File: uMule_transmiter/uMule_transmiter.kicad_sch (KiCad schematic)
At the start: 46 parts, among them J1 Test_Point_Sine, J2 Test_Point_Cos, U1 LM324, U2 LM324

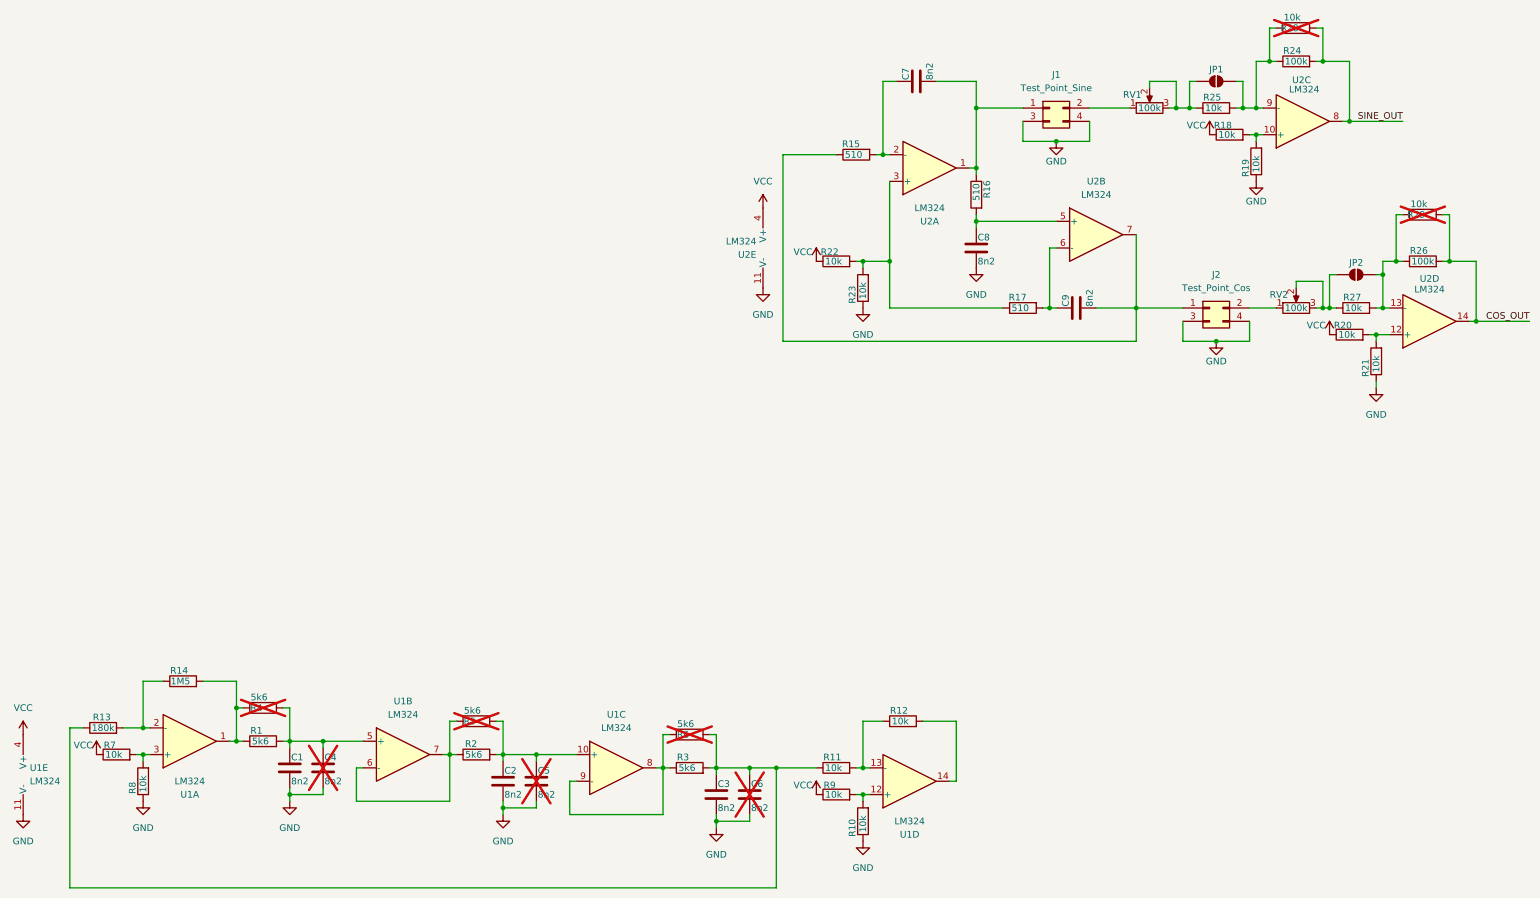
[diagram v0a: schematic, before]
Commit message: Transmiter board finnished. Ready for JLCPCB
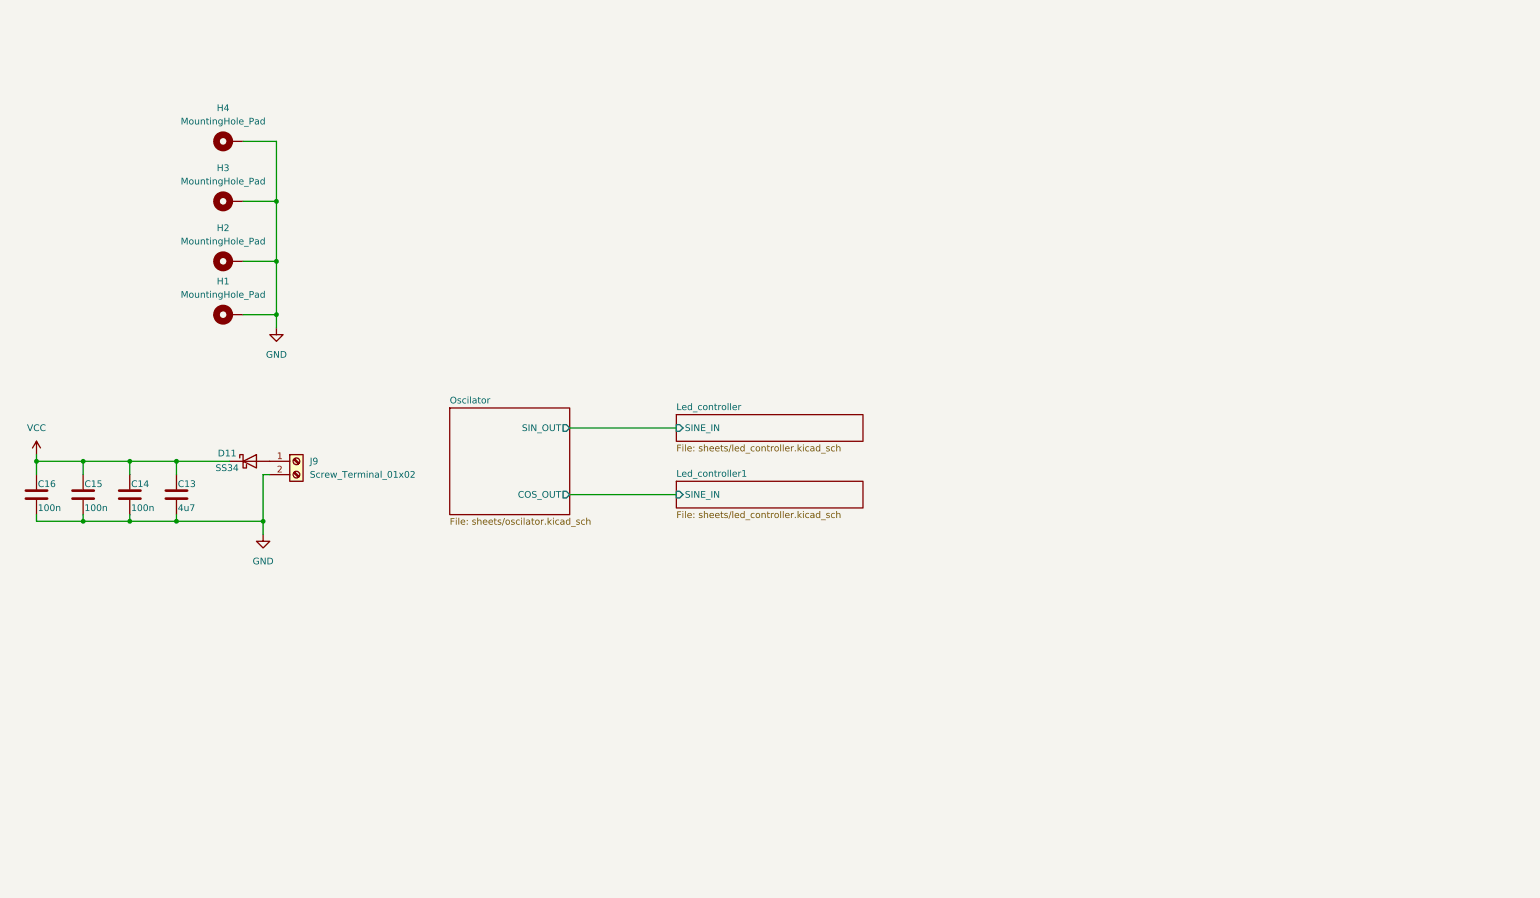
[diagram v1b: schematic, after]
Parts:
- removed C1, C2, C3, C7, C8, C9: 8n2, Capacitor_SMD:C_0603_1608Metric_Pad1.08x0.95mm_HandSolder, symbol Device:C
- removed C4, C5, C6: 8n2, Capacitor_THT:C_Axial_L5.1mm_D3.1mm_P7.50mm_Horizontal, symbol Device:C
- removed J1: Test_Point_Sine, Connector_PinHeader_2.54mm:PinHeader_2x02_P2.54mm_Vertical, symbol Connector_Generic:Conn_02x02_Odd_Even
- removed J2: Test_Point_Cos, Connector_PinHeader_2.54mm:PinHeader_2x02_P2.54mm_Vertical, symbol Connector_Generic:Conn_02x02_Odd_Even
- removed JP1, JP2: SolderJumper_2_Open, Jumper:SolderJumper-2_P1.3mm_Open_RoundedPad1.0x1.5mm, symbol Jumper:SolderJumper_2_Open
- removed R1, R2, R3: 5k6, Resistor_SMD:R_0603_1608Metric_Pad0.98x0.95mm_HandSolder, symbol Device:R
- removed R10, R11, R12, R18, R19, R20, R21, R22, R23, R25, R27, R7, R8, R9: 10k, Resistor_SMD:R_0603_1608Metric_Pad0.98x0.95mm_HandSolder, symbol Device:R
- removed R13: 180k, Resistor_THT:R_Axial_DIN0207_L6.3mm_D2.5mm_P7.62mm_Horizontal, symbol Device:R
- removed R14: 1M5, Resistor_THT:R_Axial_DIN0207_L6.3mm_D2.5mm_P7.62mm_Horizontal, symbol Device:R
- removed R15, R16, R17: 510, Resistor_SMD:R_0603_1608Metric_Pad0.98x0.95mm_HandSolder, symbol Device:R
- removed R24, R26: 100k, Resistor_SMD:R_0603_1608Metric_Pad0.98x0.95mm_HandSolder, symbol Device:R
- removed R28, R29: 10k, Resistor_THT:R_Axial_DIN0207_L6.3mm_D2.5mm_P7.62mm_Horizontal, symbol Device:R
- removed R4, R5, R6: 5k6, Resistor_THT:R_Axial_DIN0207_L6.3mm_D2.5mm_P7.62mm_Horizontal, symbol Device:R
- removed RV1, RV2: 100k, Potentiometer_THT:Potentiometer_Bourns_3266Y_Vertical, symbol Device:R_Potentiometer
- removed U1: LM324, Package_SO:SOIC-14_3.9x8.7mm_P1.27mm, symbol Amplifier_Operational:LM324
- removed U2: LM324, symbol Amplifier_Operational:LM324
- added C13: 4u7, Capacitor_SMD:C_0805_2012Metric, symbol Device:C
- added C14, C15, C16: 100n, Capacitor_SMD:C_0603_1608Metric_Pad1.08x0.95mm_HandSolder, symbol Device:C
- added D11: SS34, Diode_SMD:D_SMA, symbol Diode:SS34
- added H1, H2, H3, H4: MountingHole_Pad, MountingHole:MountingHole_3.2mm_M3_Pad_Via, symbol Mechanical:MountingHole_Pad
- added J9: Screw_Terminal_01x02, Connector_Phoenix_MC:PhoenixContact_MCV_1,5_2-G-3.5_1x02_P3.50mm_Vertical, symbol Connector:Screw_Terminal_01x02
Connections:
- net GND: now also C13.2, C14.2, C15.2, C16.2, H1.1, H2.1, H3.1, H4.1, J9.2 (Pin_2)
- net VCC: now also C13.1, C14.1, C15.1, C16.1, D11.1 (K)
- new net: D11.2 (A), J9.1 (Pin_1)
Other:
- added sheet Led_controller (sheets/led_controller.kicad_sch)
- added sheet Led_controller1 (sheets/led_controller.kicad_sch)
- added sheet Oscilator (sheets/oscilator.kicad_sch)
